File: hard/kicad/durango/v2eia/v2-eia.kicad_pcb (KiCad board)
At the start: 2 copper layers, 177.8 x 130.8 mm, 152 parts, among them J1 NANOLINK, J10 STEP, J11 EXPANSION, J2 AUDIO IN, J3 IOx, J4 LED, J605 COMPONENT VIDEO, J7 POWER IN, J706 COMPOSITE, J8 DEBUG, J9 CARTRIDGE, Q1 BC548, Q2 BC548, Q3 BC548, Q307 BC548, Q4 BC548, Q5 BC548, Q608 BC548, Q609 BC548, Q610 BC548, Q611 BC548, SW1 RESET, SW2 NMI, U003 62256, U1 65C02, U10 74HC139, U104 74HC257, U105 74HC257, U11 74HC688, U12 74HC74, U124 74HC574, U125 74HC157, U126 74HC86, U127 74HC245, U13 74HC32, U14 74HC4040, U15 74HC4040, U16 74HC02, U17 74HC21, U18 74HC85, U19 CD4040, U20 74HC85, U204 74HC257, U205 74HC257, U22 74HC175, U224 74HC166, U227 74HC20, U23 74HC86, U29 74HC139, U3 62256, U31 74HC245, U32 74HC245, U321 74HC157, U33 74HC00, U428 74HC174, U530 74HC367, U6 74HC157, U7 74HC157, U8 74HC30, U9 74HC00, X1 25.175 MHz

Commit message: fix EIA v2.2
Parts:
- added R111: 330, Resistor_THT:R_Axial_DIN0207_L6.3mm_D2.5mm_P2.54mm_Vertical, F.Cu at (171.4, 120.7)
- added R112: 330, Resistor_THT:R_Axial_DIN0207_L6.3mm_D2.5mm_P2.54mm_Vertical, F.Cu at (171.4, 113.0)
- added R113: 330, Resistor_THT:R_Axial_DIN0207_L6.3mm_D2.5mm_P2.54mm_Vertical, F.Cu at (171.4, 105.4)
- added R114: 330, Resistor_THT:R_Axial_DIN0207_L6.3mm_D2.5mm_P2.54mm_Vertical, F.Cu at (171.4, 97.8)
- JP3: value SWITCH -> POWER
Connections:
- U18 pad 11: +5V -> GND
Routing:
- net GND: track 2318.4 -> 2367.3 mm
- net DBLU: track 34.1 -> 37.9 mm
- net +5V: track 1472.1 -> 1469.6 mm
- net VA2: track 111.9 -> 113.8 mm
- net /~IOQ: track 27.4 -> 28.7 mm
- net VCLK: track 147.6 -> 148.3 mm
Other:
- board text added: "65C02 @ 1.57/3.15 MHz•32 KiB RAM•color & HIRES"
- board text added: "Durango·X Home Computer v2.2 (2024·01)"
- board text removed: "65C02 @ 1.57/3.15 MHz•32 KiB RAM•colour & HIRES"
- board text removed: "Durango·X Home Computer v2.1 (2023·12)"

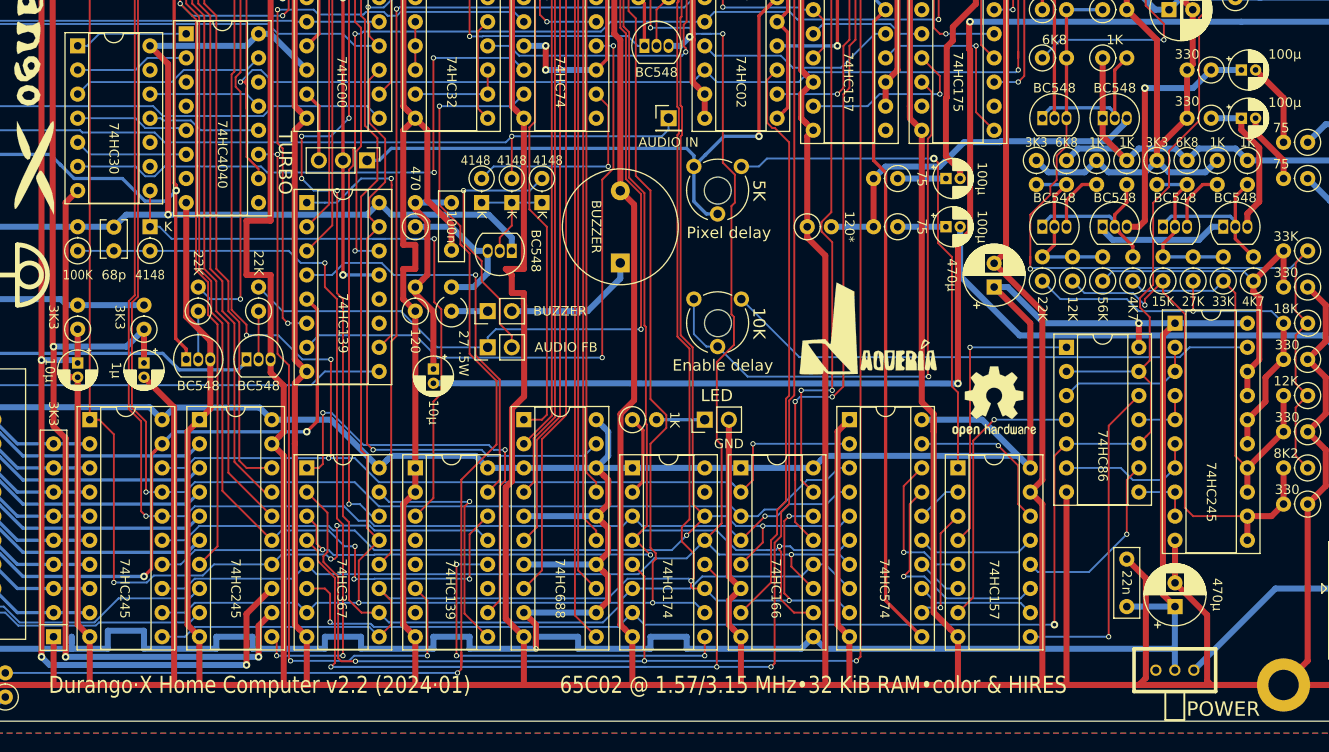
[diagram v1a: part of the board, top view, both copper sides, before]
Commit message: fix interrupt rate on EIA
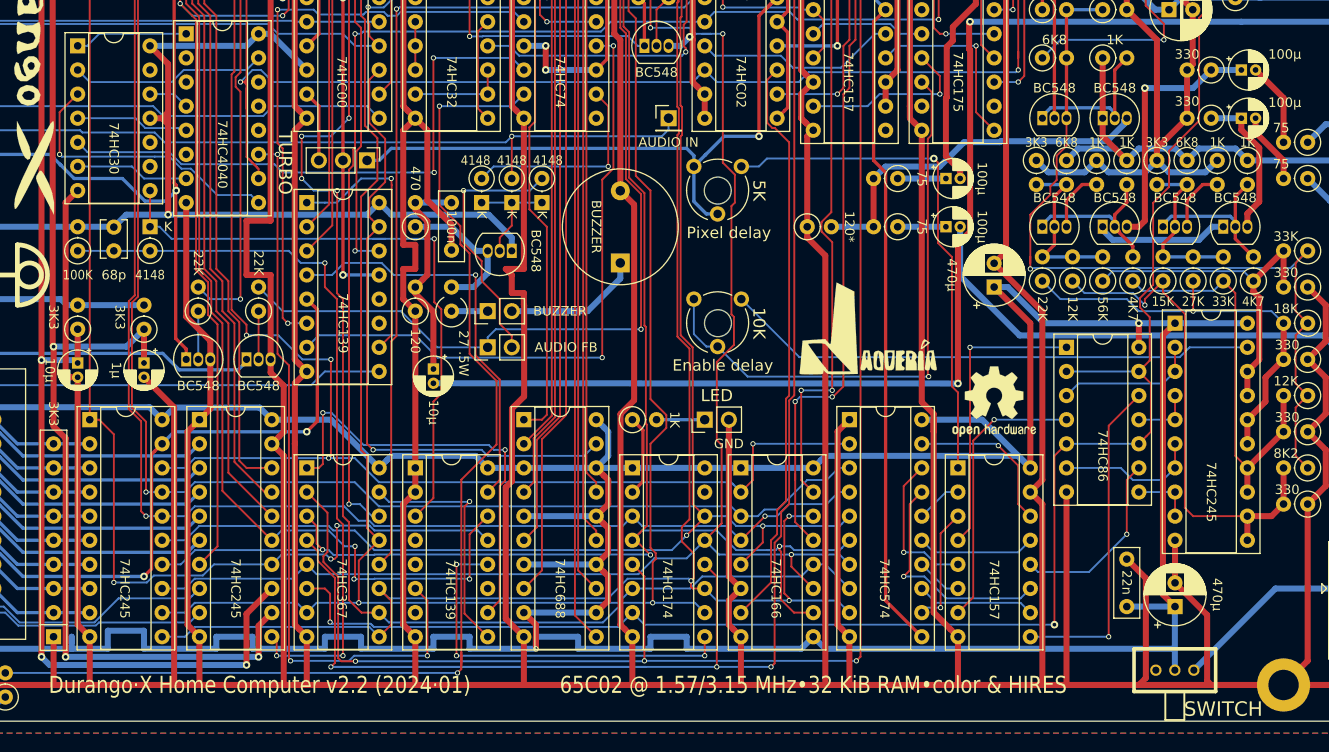
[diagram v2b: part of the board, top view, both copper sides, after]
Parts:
- JP3: value POWER -> SWITCH
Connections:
- U14 pad 12: /CNT256 -> (no net)
- U14 pad 13: /CNT128 -> (no net)
- U14 pad 2: /CNT32 -> (no net)
- U14 pad 4: (no net) -> /CNT64
- U14 pad 6: /CNT4 -> (no net)
- U14 pad 7: (no net) -> /CNT2
- U14 pad 9: (no net) -> /CNT1
- U8 pad 11: /CNT256 -> +5V
- U8 pad 12: /CNT128 -> /CNT64
- U8 pad 2: /CNT32 -> /CNT1K
- U8 pad 3: /CNT1K -> /CNT1
- U8 pad 5: /CNT4 -> /IEN
- U8 pad 6: /IEN -> /CNT2
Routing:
- net /CNT1: track 0.00 -> 30.2 mm, vias 0 -> 1
- net /CNT32: track 12.0 -> 0.00 mm
- net /CNT4: track 12.0 -> 0.00 mm
- net /CNT2: track 0.00 -> 12.0 mm
- net /CNT256: track 12.0 -> 0.00 mm
- net /CNT128: track 12.0 -> 0.00 mm
- net /CNT64: track 0.00 -> 4.34 mm
- net +5V: track 1469.6 -> 1473.3 mm

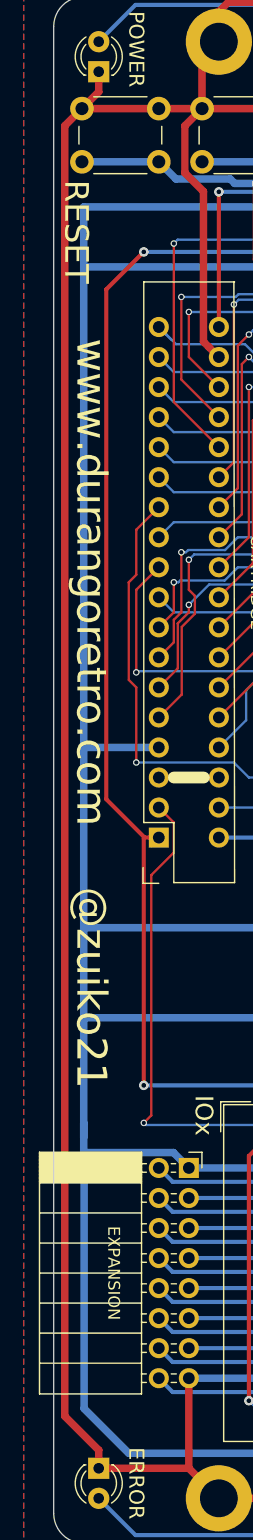
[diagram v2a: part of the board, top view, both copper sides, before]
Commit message: add LED K to EIA
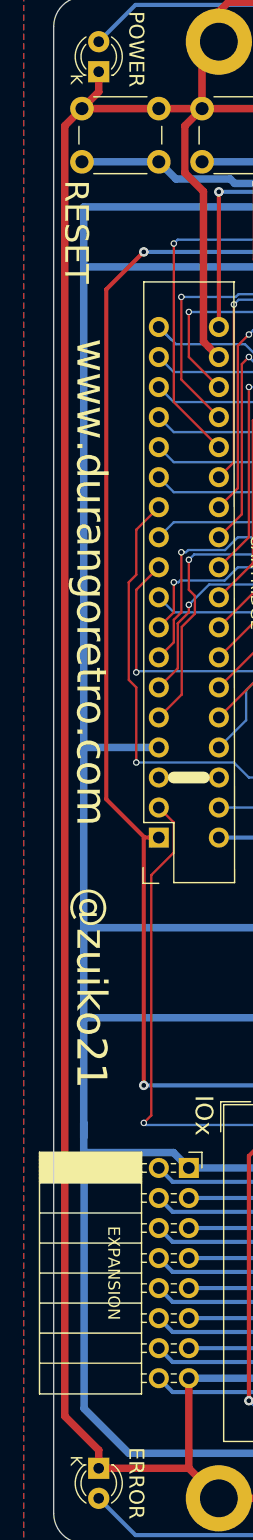
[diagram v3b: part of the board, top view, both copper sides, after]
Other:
- board text added: "K"
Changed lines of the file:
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@@
   (general
     (thickness 1.6)
-    (drawings 35)
+    (drawings 37)
     (tracks 3663)
     (zones 0)
@@
     (45 Margin user)
     (46 B.CrtYd user)
-    (47 F.CrtYd user hide)
+    (47 F.CrtYd user)
     (48 B.Fab user)
     (49 F.Fab user)
@@
     )
   )
+  (gr_text K (at 14.605 19.685 270) (layer F.SilkS)
+    (effects (font (size 1 1) (thickness 0.15)))
+  )
+  (gr_text K (at 14.605 136.525 270) (layer F.SilkS)
+    (effects (font (size 1 1) (thickness 0.15)))
+  )
   (gr_text "EIA\n(NTSC)\n60 Hz" (at 183.515 118.11 90) (layer F.SilkS)

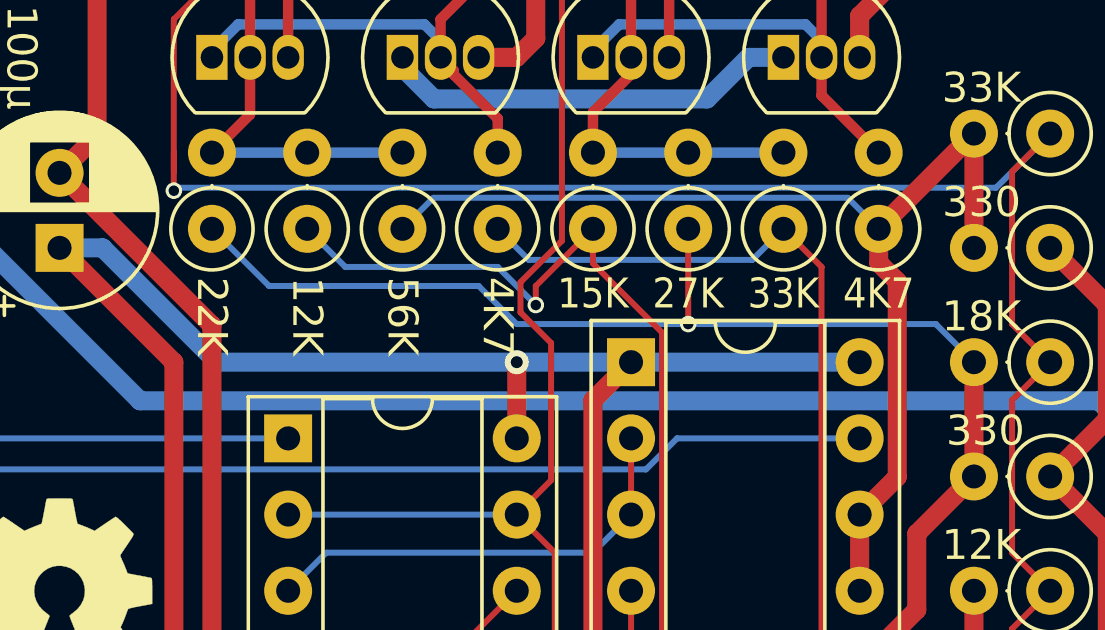
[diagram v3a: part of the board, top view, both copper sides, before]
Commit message: fix YUV values for EIA
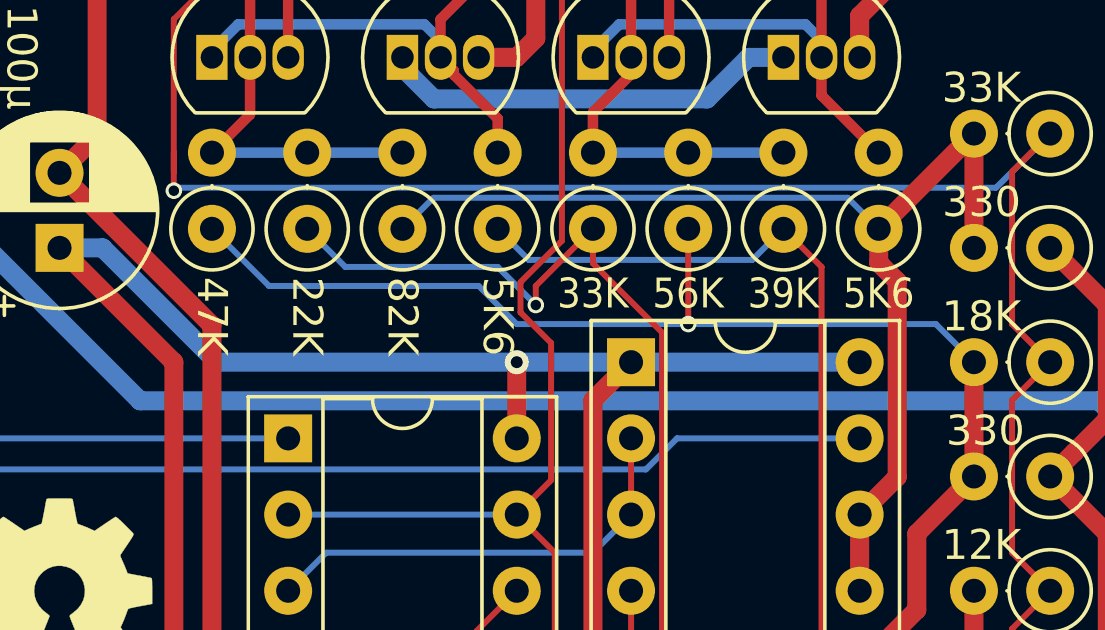
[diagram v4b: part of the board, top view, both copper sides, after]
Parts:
- R643, R653: value 4K7 -> 5K6
- R644: value 12K -> 22K
- R645: value 22K -> 47K
- R646: value 56K -> 82K
- R654: value 15K -> 33K
- R655: value 27K -> 56K
- R656: value 33K -> 39K
- renumbered R657 to R647, R647 to R657
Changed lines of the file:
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@@
     (35 F.Paste user)
     (36 B.SilkS user)
-    (37 F.SilkS user)
+    (37 F.SilkS user hide)
     (38 B.Mask user)
     (39 F.Mask user)
@@
     (45 Margin user)
     (46 B.CrtYd user)
-    (47 F.CrtYd user)
+    (47 F.CrtYd user hide)
     (48 B.Fab user)
-    (49 F.Fab user)
+    (49 F.Fab user hide)
   )
   (setup
@@
     (descr "Resistor, Axial_DIN0207 series, Axial, Vertical, pin pitch=2.54mm, 0.25W = 1/4W, length*diameter=6.3*2.5mm^2, http://cdn-reichelt.de/documents/datenblatt/B400/1_4W%23YAG.pdf")
     (tags "Resistor Axial_DIN0207 series Axial Vertical pin pitch 2.54mm 0.25W = 1/4W length 6.3mm diameter 2.5mm")
-    (fp_text reference R657 (at 1.27 1.651 unlocked) (layer B.SilkS)
+    (fp_text reference R647 (at 1.27 1.651 unlocked) (layer B.SilkS)
       (effects (font (size 1 1) (thickness 0.15)) (justify mirror))
     )
@@
       (effects (font (size 1 1) (thickness 0.15)) (justify mirror))
     )
-    (fp_text value 33K (at -2.159 0 unlocked) (layer F.SilkS)
+    (fp_text value 39K (at -2.159 0 unlocked) (layer F.SilkS)
       (effects (font (size 1 0.9) (thickness 0.15)))
     )
@@
       (effects (font (size 1 1) (thickness 0.15)) (justify mirror))
     )
-    (fp_text value 27K (at -2.159 0 unlocked) (layer F.SilkS)
+    (fp_text value 56K (at -2.159 0 unlocked) (layer F.SilkS)
       (effects (font (size 1 0.9) (thickness 0.15)))
     )
@@
       (effects (font (size 1 1) (thickness 0.15)) (justify mirror))
     )
-    (fp_text value 15K (at -2.159 0 unlocked) (layer F.SilkS)
+    (fp_text value 33K (at -2.159 0 unlocked) (layer F.SilkS)
       (effects (font (size 1 0.9) (thickness 0.15)))
     )
@@
       (effects (font (size 1 1) (thickness 0.15)) (justify mirror))
     )
-    (fp_text value 4K7 (at -2.159 0 unlocked) (layer F.SilkS)
+    (fp_text value 5K6 (at -2.159 0 unlocked) (layer F.SilkS)
       (effects (font (size 1 0.9) (thickness 0.15)))
     )
@@
     (descr "Resistor, Axial_DIN0207 series, Axial, Vertical, pin pitch=2.54mm, 0.25W = 1/4W, length*diameter=6.3*2.5mm^2, http://cdn-reichelt.de/documents/datenblatt/B400/1_4W%23YAG.pdf")
     (tags "Resistor Axial_DIN0207 series Axial Vertical pin pitch 2.54mm 0.25W = 1/4W length 6.3mm diameter 2.5mm")
-    (fp_text reference R647 (at 1.27 1.651 unlocked) (layer B.SilkS)
+    (fp_text reference R657 (at 1.27 1.651 unlocked) (layer B.SilkS)
       (effects (font (size 1 1) (thickness 0.15)) (justify mirror))
     )
@@
       (effects (font (size 1 1) (thickness 0.15)) (justify mirror))
     )
-    (fp_text value 56K (at -2.921 0 270 unlocked) (layer F.SilkS)
+    (fp_text value 82K (at -2.921 0 270 unlocked) (layer F.SilkS)
       (effects (font (size 1 1) (thickness 0.15)))
     )
@@
       (effects (font (size 1 1) (thickness 0.15)) (justify mirror))
     )
-    (fp_text value 22K (at -2.921 0 270 unlocked) (layer F.SilkS)
+    (fp_text value 47K (at -2.921 0 270 unlocked) (layer F.SilkS)
       (effects (font (size 1 1) (thickness 0.15)))
     )
@@
       (effects (font (size 1 1) (thickness 0.15)) (justify mirror))
     )
-    (fp_text value 12K (at -2.921 0 270 unlocked) (layer F.SilkS)
+    (fp_text value 22K (at -2.921 0 270 unlocked) (layer F.SilkS)
       (effects (font (size 1 1) (thickness 0.15)))
     )
@@
       (effects (font (size 1 1) (thickness 0.15)) (justify mirror))
     )
-    (fp_text value 4K7 (at -2.921 0 270 unlocked) (layer F.SilkS)
-      (effects (font (size 1 1) (thickness 0.15)))
-    )
+    (fp_text value 5K6 (at -2.921 0 270 unlocked) (layer F.SilkS)
+      (effects (font (size 1 1) (thickness 0.15)))
+    )
